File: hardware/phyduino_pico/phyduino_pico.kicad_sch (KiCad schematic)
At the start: 110 parts, among them J1 Conn_01x05, J2 Conn_01x08, J3 Conn_01x10, J4 Conn_01x06, J5 Conn_01x08, J6 632723300011, Q1 AONR21321, SW1 AYZ0102AGRLC, SW2 TL1105F250Q, U1 TPS54231DR, U2 TPS54231DR, U3 RP2040, U4 STUSB4500QTR, U5 MAX11635EEE+T, U6 W25Q128JVPIQ TR, U7 LM4040DIM3-2.0/NOPB, Y1 H130B-12.000-18-3030-TR

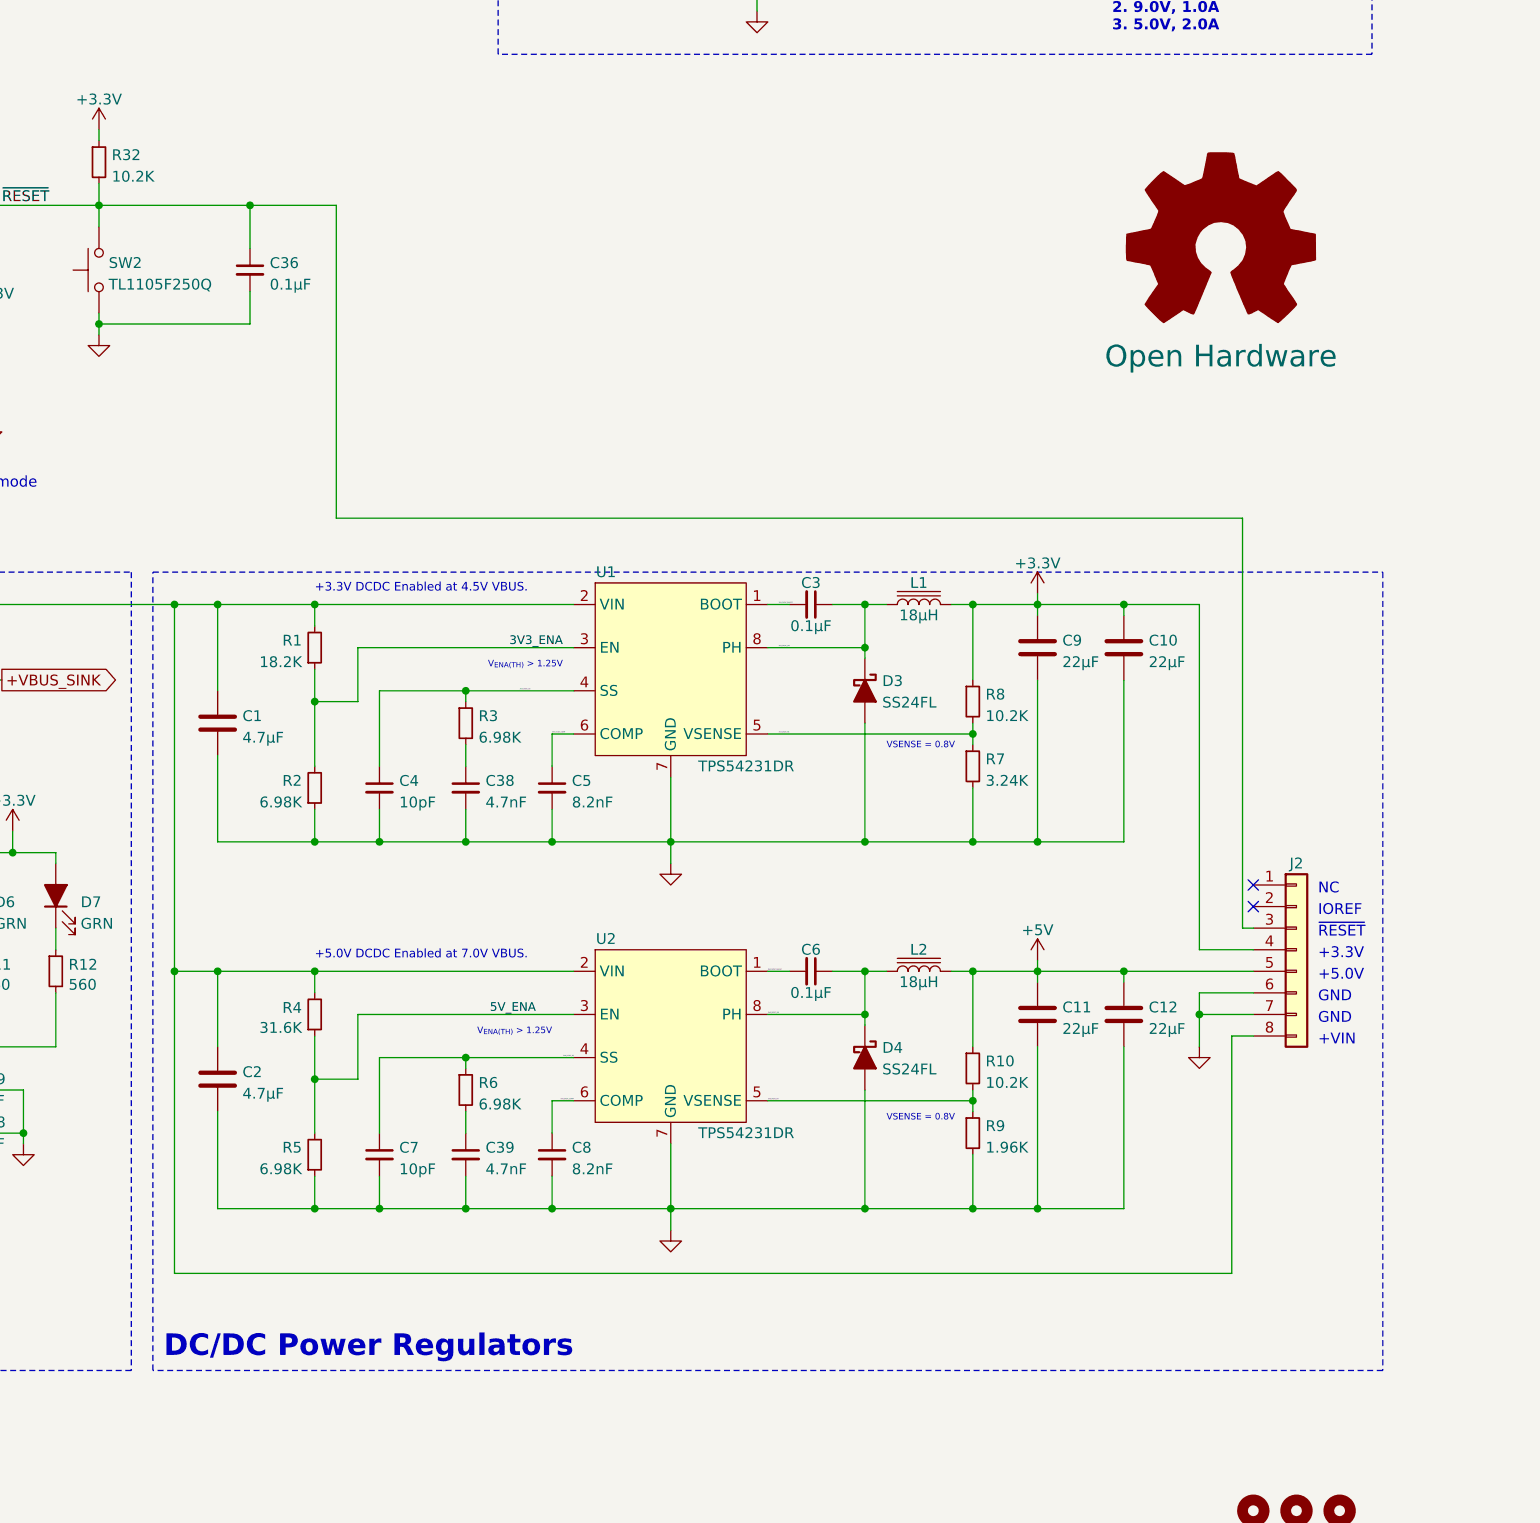
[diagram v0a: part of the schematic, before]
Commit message: Hardware projects added
Final boards added to repository : Phyduino Pico Rev C and Analog Front End Rev C. includes symbol and front print libraries for each project.
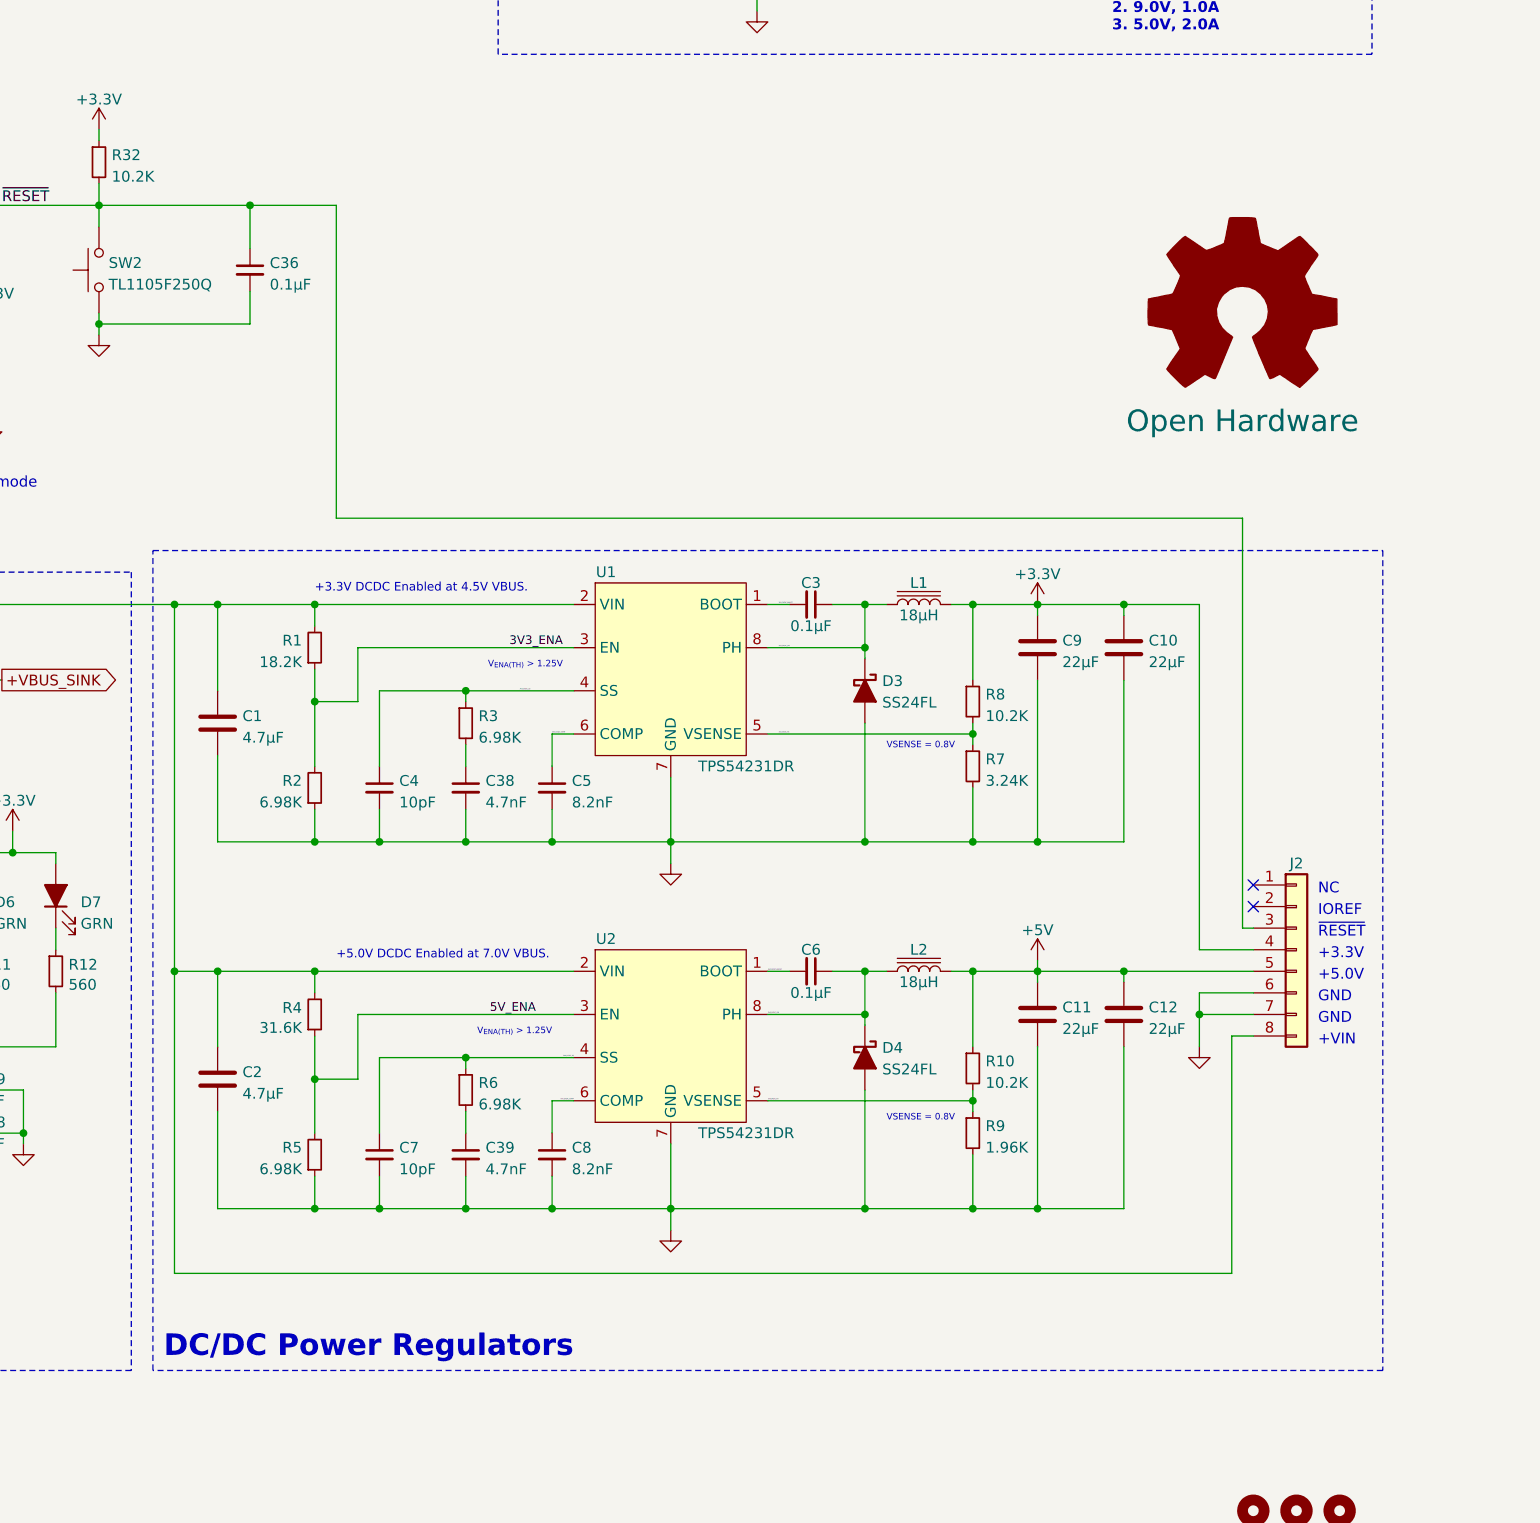
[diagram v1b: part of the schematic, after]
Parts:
- C1, C2: symbol Device:C -> phyduino_pico:C; Dist_PN (none) -> 963-GMK325BJ475KN-T; Distributor (none) -> Mouser; Variant (none) -> STUDENT
- C10, C11, C12, C9: symbol Device:C -> phyduino_pico:C; Dist_PN (none) -> 187-CL21A226MAYNNNE; Distributor (none) -> Mouser; Variant (none) -> STUDENT
- C13, C15: symbol Device:C_Small -> phyduino_pico:C_Small; Dist_PN (none) -> 603-CC402JRNPO9BN270; Distributor (none) -> Mouser; Variant (none) -> ADV_SMT
- C14, C16, C18, C20, C21, C22, C23, C24, C25, C26, C30: symbol Device:C_Small -> phyduino_pico:C_Small; Dist_PN (none) -> 603-CC402KRX5R9BB104; Distributor (none) -> Mouser; Variant (none) -> ADV_SMT
- C17, C19, C28, C29, C32: symbol Device:C_Small -> phyduino_pico:C_Small; Dist_PN (none) -> 81-GRM155R6YA105KE1D; Distributor (none) -> Mouser; Variant (none) -> ADV_SMT
- C27, C3, C31, C34, C36, C6: symbol Device:C_Small -> phyduino_pico:C_Small; Dist_PN (none) -> 80-C0805C104Z5V; Distributor (none) -> Mouser; Variant (none) -> STUDENT
- C33: symbol Device:C_Small -> phyduino_pico:C_Small; Dist_PN (none) -> 187-CL21B105MBFNNNE; Distributor (none) -> Mouser; Variant (none) -> STUDENT
- C35: symbol Device:C -> phyduino_pico:C; Dist_PN (none) -> 603-CC402KRX5R9BB104; Distributor (none) -> Mouser; Variant (none) -> ADV_SMT
- C37: footprint Capacitor_SMD:C_0805_2012Metric -> Capacitor_SMD:C_0805_2012Metric_Pad1.18x1.45mm_HandSolder; symbol Device:C_Small -> phyduino_pico:C_Small; Dist_PN (none) -> 80-C0805C104Z5V; Distributor (none) -> Mouser; Variant (none) -> STUDENT
- C38, C39: symbol Device:C_Small -> phyduino_pico:C_Small; Dist_PN (none) -> 187-CL21B472KBANNNC; Distributor (none) -> Mouser; Variant (none) -> STUDENT
- C4, C7: symbol Device:C_Small -> phyduino_pico:C_Small; Dist_PN (none) -> 187-CL21C100CBANNNC; Distributor (none) -> Mouser; Variant (none) -> STUDENT
- C5, C8: symbol Device:C_Small -> phyduino_pico:C_Small; Dist_PN (none) -> 80-C0805C822K5R; Distributor (none) -> Mouser; Variant (none) -> STUDENT
- D1: symbol Device:LED_Filled -> phyduino_pico:LED_Filled; Dist_PN 475-1278-1-ND -> 720-LSR976-NR-1; Distributor (none) -> Mouser; Variant (none) -> STUDENT
- D2: symbol Device:LED_Filled -> phyduino_pico:LED_Filled; Dist_PN 475-2560-1-ND -> 720-LYR976-PS-36; Distributor (none) -> Mouser; Variant (none) -> STUDENT
- D3, D4: symbol Device:D_Schottky_Filled -> phyduino_pico:D_Schottky_Filled; Dist_PN (none) -> 512-SS24FL; Distributor (none) -> Mouser; PN (none) -> ${VALUE}; Variant (none) -> STUDENT
- D5, D8: symbol Device:LED_Filled -> phyduino_pico:LED_Filled; Distributor (none) -> Digikey; Variant (none) -> STUDENT
- D6, D7: symbol Device:LED_Filled -> phyduino_pico:LED_Filled; Dist_PN 732-11992-1-ND -> 710-150040VS73240; Distributor (none) -> Mouser; Variant (none) -> ADV_SMT
- FB1: value FerriteBead_Small -> BLM15AG221SH1D; symbol Device:FerriteBead_Small -> phyduino_pico:FerriteBead_Small; Dist_PN (none) -> 81-BLM15GG221SN1D; Distributor (none) -> Mouser; PN (none) -> ${VALUE}; Variant (none) -> ADV_SMT
- H1, H2, H3: symbol Mechanical:MountingHole -> phyduino_pico:MountingHole
- J1: symbol Connector_Generic:Conn_01x05 -> phyduino_pico:Conn_01x05; Dist_PN (none) -> 855-M20-7820546; Distributor (none) -> Mouser; PN (none) -> M20-7820546; Variant (none) -> STUDENT
- J2, J5: symbol Connector_Generic:Conn_01x08 -> phyduino_pico:Conn_01x08; Dist_PN (none) -> 855-M20-7820842; Distributor (none) -> Mouser; PN (none) -> M20-7820842; Variant (none) -> STUDENT
- J3: symbol Connector_Generic:Conn_01x10 -> phyduino_pico:Conn_01x10; Dist_PN (none) -> 952-1847-ND; Distributor (none) -> Digikey; PN (none) -> M20-7821046; Variant (none) -> STUDENT
- J4: symbol Connector_Generic:Conn_01x06 -> phyduino_pico:Conn_01x06; Dist_PN (none) -> 855-M20-7820642; Distributor (none) -> Mouser; PN (none) -> M20-7820642; Variant (none) -> STUDENT
- J6: symbol Connectors - USB:632723100011 -> phyduino_pico:632723100011; DIST_PN 732-9618-1-ND -> (none); Dist_PN (none) -> 710-632723300011; Distributor (none) -> Mouser; PN (none) -> ${VALUE}; Variant (none) -> ADV_SMT
- L1, L2: symbol Device:L_Iron -> phyduino_pico:L_Iron; Dist_PN (none) -> 994-MSS1246-183MLC; Distributor (none) -> Mouser; Variant (none) -> STUDENT
- Q1: symbol Transistor - MOSFET:AONR21321 -> phyduino_pico:AONR21321; Dist_PN (none) -> 785-1797-1-ND; Distributor (none) -> Digikey; PN (none) -> ${VALUE}; Variant (none) -> ADV_SMT
- R1: symbol Device:R_Small -> phyduino_pico:R_Small; Dist_PN (none) -> 603-RC0805FR-0718K2L; Distributor (none) -> Mouser; Variant (none) -> STUDENT
- R10, R14, R32, R8: symbol Device:R_Small -> phyduino_pico:R_Small; Dist_PN (none) -> 603-RC0805FR-0710K2L; Distributor (none) -> Mouser; Variant (none) -> STUDENT
- R11, R12: symbol Device:R_Small -> phyduino_pico:R_Small; Dist_PN (none) -> 603-RC0402FR-13560RL; Distributor (none) -> Mouser; Variant (none) -> ADV_SMT
- R13, R16, R17, R20, R38, R39: symbol Device:R_Small -> phyduino_pico:R_Small; Dist_PN (none) -> 603-AC0402FR-074K7L; Distributor (none) -> Mouser; Variant (none) -> ADV_SMT
- R15: symbol Device:R_Small -> phyduino_pico:R_Small; Dist_PN (none) -> 603-RC0805FR-13100KL; Distributor (none) -> Mouser; Variant (none) -> STUDENT
- R18, R19: symbol Device:R_Small -> phyduino_pico:R_Small; Dist_PN (none) -> 603-AC0402FR-0727RL; Distributor (none) -> Mouser; Variant (none) -> ADV_SMT
- R2, R3, R5, R6: symbol Device:R_Small -> phyduino_pico:R_Small; Dist_PN (none) -> 603-RC0805FR-076K98L; Distributor (none) -> Mouser; Variant (none) -> STUDENT
- R21, R22: symbol Device:R_Small -> phyduino_pico:R_Small; Dist_PN (none) -> 603-AC0402FR-075K1L; Distributor (none) -> DNP; Variant (none) -> ADV_SMT
- R23: symbol Device:R_Small -> phyduino_pico:R_Small; Dist_PN (none) -> 603-RC0805FR-07124RL; Distributor (none) -> Mouser; Variant (none) -> STUDENT
- R24, R25: symbol Device:R_Small -> phyduino_pico:R_Small; Dist_PN (none) -> 603-RC0402FR-131KL; Distributor (none) -> Mouser; Variant (none) -> ADV_SMT
- R26: symbol Device:R_Small -> phyduino_pico:R_Small; Dist_PN (none) -> 603-RC0402FR-07100KL; Distributor (none) -> Mouser; Variant (none) -> ADV_SMT
- R27: symbol Device:R_Small -> phyduino_pico:R_Small; Dist_PN (none) -> 603-RC0402FR-0722KL; Distributor (none) -> Mouser; Variant (none) -> ADV_SMT
- R28: symbol Device:R_Small -> phyduino_pico:R_Small; Dist_PN (none) -> 603-RC0402FR-072KL; Distributor (none) -> Mouser; Variant (none) -> ADV_SMT
- R29: symbol Device:R_Small -> phyduino_pico:R_Small; Dist_PN (none) -> 603-RC0402FR-07100RL; Distributor (none) -> Mouser; Variant (none) -> ADV_SMT
- R30: symbol Device:R_Small -> phyduino_pico:R_Small; Dist_PN (none) -> 603-RC0805FR-07560RL; Distributor (none) -> Mouser; Variant (none) -> STUDENT
- R31: symbol Device:R_Small -> phyduino_pico:R_Small; Dist_PN (none) -> 603-RC0805FR-071ML; Distributor (none) -> Mouser; Variant (none) -> STUDENT
- R33, R34, R35: symbol Device:R_Small -> phyduino_pico:R_Small; Dist_PN (none) -> 603-RC0805FR-131KL; Distributor (none) -> Mouser; Variant (none) -> STUDENT
- R36: symbol Device:R_Small -> phyduino_pico:R_Small; Dist_PN (none) -> 603-RC0805FR-07649RL; Distributor (none) -> Mouser; Variant (none) -> STUDENT
- R37: symbol Device:R_Small -> phyduino_pico:R_Small; Dist_PN (none) -> 603-RC0805FR-0711K5L; Distributor (none) -> Mouser; Variant (none) -> STUDENT
- R4: symbol Device:R_Small -> phyduino_pico:R_Small; Dist_PN (none) -> 603-RC0805FR-0731K6L; Distributor (none) -> Mouser; Variant (none) -> STUDENT
- R7: symbol Device:R_Small -> phyduino_pico:R_Small; Dist_PN (none) -> 603-RC0805FR-073K24L; Distributor (none) -> Mouser; Variant (none) -> STUDENT
- R9: symbol Device:R_Small -> phyduino_pico:R_Small; Dist_PN (none) -> 603-RC0805FR-071K96L; Distributor (none) -> Mouser; Variant (none) -> STUDENT
- SW1: symbol Switch:SW_SPDT -> phyduino_pico:SW_SPDT; Dist. PN 401-2012-1-ND -> (none); Dist_PN (none) -> 611-AYZ0102AGRLC; Distributor (none) -> Mouser; PN (none) -> ${VALUE}; Variant (none) -> STUDENT
- SW2: symbol Switch:SW_Push -> phyduino_pico:SW_Push; Dist_PN (none) -> 612-TL1105-250; Distributor (none) -> Mouser; PN (none) -> ${VALUE}; Variant (none) -> STUDENT
- U1, U2: symbol PMIC_DCDC:TPS54231DR -> phyduino_pico:TPS54231DR; Dist_PN (none) -> 595-TPS54231DR; Distributor (none) -> Mouser; PN (none) -> ${VALUE}; Variant (none) -> STUDENT
- U3: symbol Digital_Microcontrollers:RP2040 -> phyduino_pico:RP2040; Dist_PN (none) -> 358-SC09147; Distributor (none) -> Mouser; PN (none) -> SC0914(13); Variant (none) -> ADV_SMT
- U4: symbol Interface_USB:STUSB4500QTR -> phyduino_pico:STUSB4500QTR; Dist_PN (none) -> 511-STUSB4500QTR; Distributor (none) -> Mouser; PN (none) -> ${VALUE}; Variant (none) -> ADV_SMT
- U5: symbol Analog - ADC:MAX11635EEE+T -> phyduino_pico:MAX11635EEE+T; Dist_PN (none) -> 700-MAX11635EEE+; Distributor (none) -> Mouser; PN (none) -> ${VALUE}; Variant (none) -> STUDENT
- U6: symbol Memory_Flash:W25Q32JVZP -> phyduino_pico:W25Q32JVZP; Dist_PN (none) -> 454-W25Q128JVPIQTR; Distributor (none) -> Mouser; PN (none) -> ${VALUE}; Variant (none) -> ADV_SMT
- U7: symbol Reference_Voltage:LM4040DBZ-2.0 -> phyduino_pico:LM4040DBZ-2.0; Dist_PN (none) -> 595-M4040DIM3-2.0NPB; Distributor (none) -> Mouser; PN (none) -> ${VALUE}; Variant (none) -> STUDENT
- Y1: symbol Device:Crystal_GND24 -> phyduino_pico:Crystal_GND24; Dist_PN (none) -> 2151-H130B-12.000-18-3030-TRCT-ND; Distributor (none) -> Digikey; PN (none) -> ${VALUE}; Variant (none) -> ADV_SMT
- Z1: symbol Device:D_Zener_Filled -> phyduino_pico:D_Zener_Filled; Dist_PN (none) -> 504-SMFE20A; Distributor (none) -> Mouser; PN (none) -> ${VALUE}; Variant (none) -> ADV_SMT
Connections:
- net +3V3 renamed +3.3V

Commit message: Part Number update
Updated part numbers
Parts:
- Y1: value H130B-12.000-18-3030-TR -> ABM8AIG-12.000MHz-2-T

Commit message: Phyduino PICO KiCAD project updated, REV D
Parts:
- added C14: 0.1µF, Capacitor_SMD:C_0402_1005Metric_Pad0.74x0.62mm_HandSolder, symbol Device:C_Small
- added C41, C42, C43, C44: 10,000pF, Capacitor_SMD:C_0402_1005Metric_Pad0.74x0.62mm_HandSolder, symbol phyduino_pico:C_Small
- added DRAW1: Open Hardware, Symbol:OSHW-Logo2_9.8x8mm_SilkScreen, symbol Graphic:Logo_Open_Hardware_Large
- added R13: 42.2KΩ, Resistor_SMD:R_0402_1005Metric_Pad0.72x0.64mm_HandSolder, symbol Device:R_Small
- added R21 (x2): 19.6KΩ, Resistor_SMD:R_0402_1005Metric_Pad0.72x0.64mm_HandSolder, symbol Device:R_Small
- added R21 (x2): 4.7KΩ, Resistor_SMD:R_0402_1005Metric_Pad0.72x0.64mm_HandSolder, symbol Device:R_Small
- added R47, R48, R49, R50: 10Ω, Resistor_SMD:R_0402_1005Metric_Pad0.72x0.64mm_HandSolder, symbol phyduino_pico:R_Small
- added R51, R52, R53: 100KΩ, Resistor_SMD:R_0402_1005Metric_Pad0.72x0.64mm_HandSolder, symbol phyduino_pico:R_Small
- added U8: TPS2121RUXT, Package Lib - QFN:VQFN-HR-12, symbol PMIC - TI:TPS2121RUX
- added U9: USBLC6-2P6, Package_TO_SOT_SMD:SOT-666, symbol Protection - Signal:USBLC6-2P6
- C1, C2: Manufacturer (none) -> Taiyo Yuden; PN (none) -> GMK325BJ475KN-T
- C10, C11, C12, C9: Manufacturer (none) -> Samsung Electro-Mechanics; PN (none) -> CL21A226MAYNNNE
- C13, C15: Manufacturer (none) -> Yageo; PN (none) -> CC0402JRNPO9BN270
- C14, C16, C18, C20, C21, C22, C23, C24, C25, C26, C30, C35: Manufacturer (none) -> Yageo; PN (none) -> CL05A104KA5NNNC
- C17, C19, C28, C29, C32: Manufacturer (none) -> Murata Electronics; PN (none) -> GRM155R6YA105KE1D
- C27, C3, C31, C34, C36, C37, C6: Manufacturer (none) -> KEMET; PN (none) -> C0805C104Z5V
- C33: Manufacturer (none) -> Samsung Electro-Mechanics; PN (none) -> CL21B105MBFNNNE
- C38, C39: Manufacturer (none) -> Samsung Electro-Mechanics; PN (none) -> CL21B472KBANNNC
- C4, C7: Manufacturer (none) -> Samsung Electro-Mechanics; PN (none) -> CL21C100CBANNNC
- C5, C8: Manufacturer (none) -> KEMET; PN (none) -> C0805C822K5RAC7800
- D1, D2, D5, D8: Manufacturer (none) -> ams-OSRAM USA INC.
- D3, D4: Manufacturer (none) -> ONSemi
- D6, D7: Manufacturer (none) -> Wurth Elektronik
- FB1: Manufacturer (none) -> Murata Electronics
- J1, J2, J3, J4, J5: Manufacturer (none) -> Harwin Inc.
- L1, L2: Manufacturer (none) -> Coilcraft
- Q1: Manufacturer (none) -> Alpha & Omega Semiconductor Inc.
- R1: value 18.2K -> 18.2KΩ; Manufacturer (none) -> YAGEO; PN (none) -> RC0805FR-0718K2L
- R10, R14, R32, R8: value 10.2K -> 10.2KΩ; Manufacturer (none) -> YAGEO; PN (none) -> RC0805FR-0710K2L
- R11, R12: Manufacturer (none) -> Yageo; PN (none) -> RC0402FR-13560RL
- R13, R16, R20: value 4.7K -> 4.7KΩ; Manufacturer (none) -> Yageo; PN (none) -> AC0402FR-074K7L; now fitted
- R15: value 100K -> 100KΩ; Manufacturer (none) -> YAGEO; PN (none) -> RC0805FR-13100KL
- R17, R38, R39: value 4.7K -> 4.7KΩ; Manufacturer (none) -> Yageo; PN (none) -> AC0402FR-074K7L
- R18, R19: value 27 -> 27Ω; Manufacturer (none) -> Yageo; PN (none) -> AC0402FR-0727RL
- R2, R3, R5, R6: value 6.98K -> 6.98KΩ; Manufacturer (none) -> YAGEO; PN (none) -> RC0805FR-076K98L
- R21, R22: Manufacturer (none) -> Yageo; PN (none) -> AC0402FR-075K1L
- R23: value 124 -> 124Ω; Manufacturer (none) -> YAGEO; PN (none) -> RC0805FR-07124RL
- R24, R25: value 1K -> 1KΩ; Manufacturer (none) -> Yageo; PN (none) -> RC0402FR-131KL
- R26: value 100K -> 100KΩ; Manufacturer (none) -> Yageo; PN (none) -> RC0402FR-07100KL
- R27: value 22K -> 22KΩ; Manufacturer (none) -> Yageo; PN (none) -> RC0402FR-0722KL
- R28: value 2.0K -> 2.0KΩ; Manufacturer (none) -> Yageo; PN (none) -> RC0402FR-072KL
- R29: value 100 -> 100Ω; Manufacturer (none) -> Yageo; PN (none) -> RC0402FR-07100RL
- R30: value 560 -> 560Ω; Manufacturer (none) -> YAGEO; PN (none) -> RC0805FR-07560RL
- R31: value 1M -> 1MΩ; Manufacturer (none) -> YAGEO; PN (none) -> RC0805FR-071ML
- R33, R34, R35: value 1K -> 1KΩ; Manufacturer (none) -> YAGEO; PN (none) -> RC0805FR-131KL
- R36: value 649 -> 649Ω; Manufacturer (none) -> YAGEO; PN (none) -> RC0805FR-07649RL
- R37: value 2K -> 2KΩ; Manufacturer (none) -> YAGEO; PN (none) -> RC0805FR-0711K5L
- R4: value 31.6K -> 31.6KΩ; Manufacturer (none) -> YAGEO; PN (none) -> RC0805FR-0731K6L
- R7: value 3.24K -> 3.24KΩ; Manufacturer (none) -> YAGEO; PN (none) -> RC0805FR-073K24L
- R9: Manufacturer (none) -> YAGEO; PN (none) -> RC0805FR-071K96L
- SW1: Manufacturer (none) -> C&K
- SW2: Manufacturer (none) -> E-Switch
- U1, U2, U7: Manufacturer (none) -> Texas Instruments
- U3: Manufacturer (none) -> Raspberry Pi
- U4: Manufacturer (none) -> ST Microelectronics
- U5: Manufacturer (none) -> Analog Devices Inc./Maxim Integrated
- U6: Manufacturer (none) -> Winbond Electronics
- Y1: value ABM8AIG-12.000MHz-2-T -> H130B-12.000-18-3030-TR; Manufacturer (none) -> Raltron Electronics
- Z1: Manufacturer (none) -> Eaton - Electronics Division
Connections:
- net +3.3V: now also U9.5 (VBUS)
- net +5V: now also U8.1 (OUT), U8.8 (OUT); no longer C11.1, C12.1, L2.2, R10.1
- net A3: now also R49.2, R51.2; no longer U5.1 (AIN0)
- net A4: now also R50.2, R52.2; no longer U5.2 (AIN1)
- net A5: now also R48.2, R53.2; no longer U5.3 (AIN2)
- net GND: now also C37.2, C14.2, C41.2, C42.2, C43.2, C44.2, R13.1, R21.1, R21.1, R51.1, R52.1, R53.1, U8.12 (GND), U8.3 (CP2), U8.6 (PR1), U8.9 (ST), U9.2 (GND)
- net GNDPWR: now also R31.1
- net USB_D_N: now also U9.4 (I/O2); no longer R19.2
- net USB_D_P: now also U9.6 (I/O1); no longer R18.2
- net VBUS_MONITOR: now also R47.2; no longer U5.4 (AIN3)
- net +VBUS renamed +VBUS_SRC
- net +VBUS_SINK renamed VBUS
- net VBUS: now also R21.2, U8.2 (IN2)
- removed net CHGND_2_SGND: C37.2, R31.1
- new net AIN0_A3: C43.1, R49.1, U5.1 (AIN0)
- new net AIN1_A4: C44.1, R50.1, U5.2 (AIN1)
- new net AIN2_A5: C42.1, R48.1, U5.3 (AIN2)
- new net AIN3_VBUS: C41.1, R47.1, U5.4 (AIN3)
- new net DCDC_5VOUT: C11.1, C12.1, L2.2, R10.1, R21.2, U8.7 (IN1)
- new net PMUX_LIM: R13.2, U8.10 (ILM)
- new net PMUX_OV1: R21.1, R21.2, U8.5 (OV1)
- new net PMUX_OV2: R21.1, R21.2, U8.4 (OV2)
- new net PMUX_SS: C14.1, U8.11 (SS)
- new net USB_SP_D_N: R19.2, U9.3 (I/O2)
- new net USB_SP_D_P: R18.2, U9.1 (I/O1)
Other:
- note added: "+3.3V DCDC Enabled at 4.5V +V_{BUS}."
- note added: "+5.0V DCDC Enabled at 7.0V +V_{BUS}."
- note added: ">1.06V"
- note added: "A3"
- note added: "A4"
- note added: "A5"
- note added: "Board USB Power Delivery Profiles (10W_{MAX}) Profile 1: +5.0V, 2.0A => POK2 = OFF, POK3 = OFF Profile 2: +9.0V, 1.0A => POK2 = ON, POK3 = OFF Profile 3: +20.0V, 0.5A => POK2 = OFF, POK3 = ON"
- note added: "D6 = POK2 D7 = POK3"
- note added: "I_{LIMIT} = 2.6A"
- note added: "Raspberry PI Pico Microcontroller"
- note added: "Selection of IN2 is disabled once +V_{BUS} is above +5.5V. Only +5V will be presented to the output pin."
- note removed: "+3.3V DCDC Enabled at 4.5V VBUS."
- note removed: "+5.0V DCDC Enabled at 7.0V VBUS."
- note removed: "Board USB Power Delivery Profiles 1. 20.0V, 0.5A 2. 9.0V, 1.0A 3. 5.0V, 2.0A"
- note removed: "Each LED will turn on if the power supply is active. D1 should always be on when +V_{BUS} is applied. +3.3V LED (D2) will turn on when +V_{BUS} > 4.5V and +5.0V LED (D5) will turn on when +V_{BUS} > 7.0V."
- moved on the sheet: C1, C10, C11, C12, C13, C14, C15, C16, C17, C18, C19, C2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
